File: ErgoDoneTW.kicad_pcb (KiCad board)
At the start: 2 copper layers, 182.8 x 158.9 mm, 71 parts, among them J1 3.5mm, J2 USB_C, P1 hole_r1.75, P2 hole_r1.75, P3 hole_r1.75, P4 hole_r1.75, P5 hole_r1.75, P6 hole_r1.75, P7 hole_r1.75, P8 hole_r1.75, SW0:10 SW0:3, SW0:11 SW0:2, SW0:12 SW0:1, SW0:7 SW0:6, SW0:8 SW0:5, SW0:9 SW0:4, SW1:10 SW1:3, SW1:11 SW1:2, SW1:12 SW1:1, SW1:13 SW1:0, SW1:9 SW1:4, SW2:10 SW2:3, SW2:11 SW2:2, SW2:12 SW2:1, SW2:13 SW2:0, SW2:7 SW2:6, SW2:8 SW2:5, SW2:9 SW2:4, SW3:10 SW3:3, SW3:11 SW3:2, SW3:12 SW3:1, SW3:13 SW3:0, SW3:8 SW3:5, SW3:9 SW3:4, SW4:10 SW4:3, SW4:11 SW4:2, SW4:12 SW4:1, SW4:13 SW4:0, SW4:7 SW4:6, SW4:8 SW4:5, SW4:9 SW4:4, SW5:10 SW5:3, SW5:11 SW5:2, SW5:12 SW5:1, SW5:13 SW5:0, SW5:7 SW5:6, SW5:8 SW5:5, SW5:9 SW5:4, U2 MCP23018, U4 TEENSY2.0

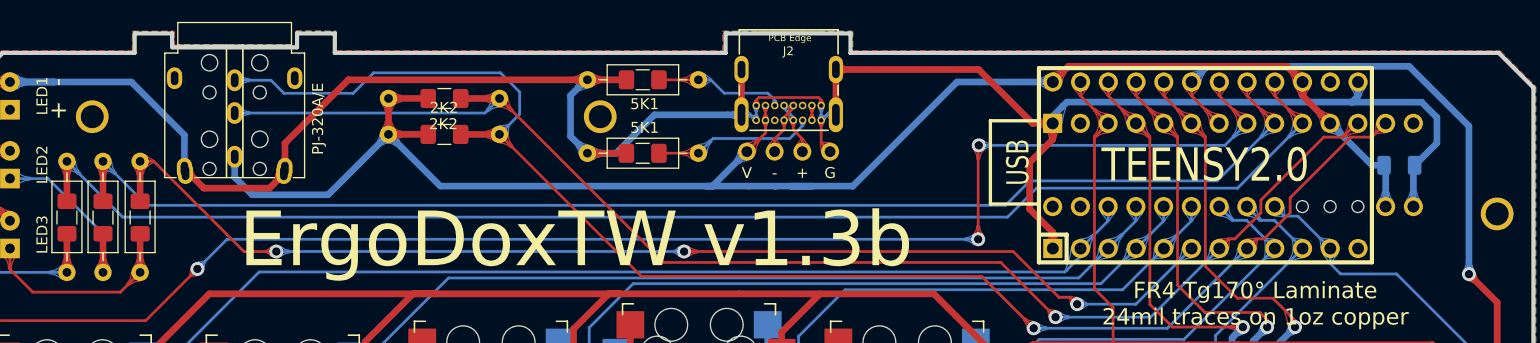
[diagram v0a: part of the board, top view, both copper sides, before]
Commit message: update smd  cap position to avoid conflict with mcp23018
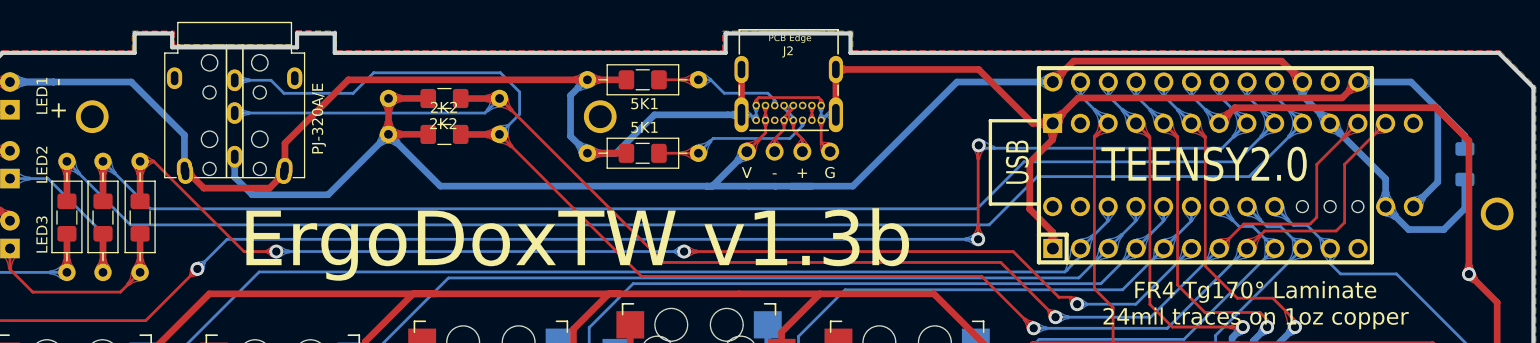
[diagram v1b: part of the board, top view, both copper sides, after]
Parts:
- moved 100nF 6.00 mm to (199.6, 42.5), turned to 90 degrees
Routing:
- net VCC: track 148.6 -> 160.0 mm
- net /ROW1: track 350.7 -> 345.8 mm
- net GND: track 227.6 -> 231.9 mm
- net /SDAM: track 133.3 -> 135.6 mm
- net /SCLM: track 123.6 -> 125.8 mm
- net /LED_A: track 127.2 -> 127.8 mm

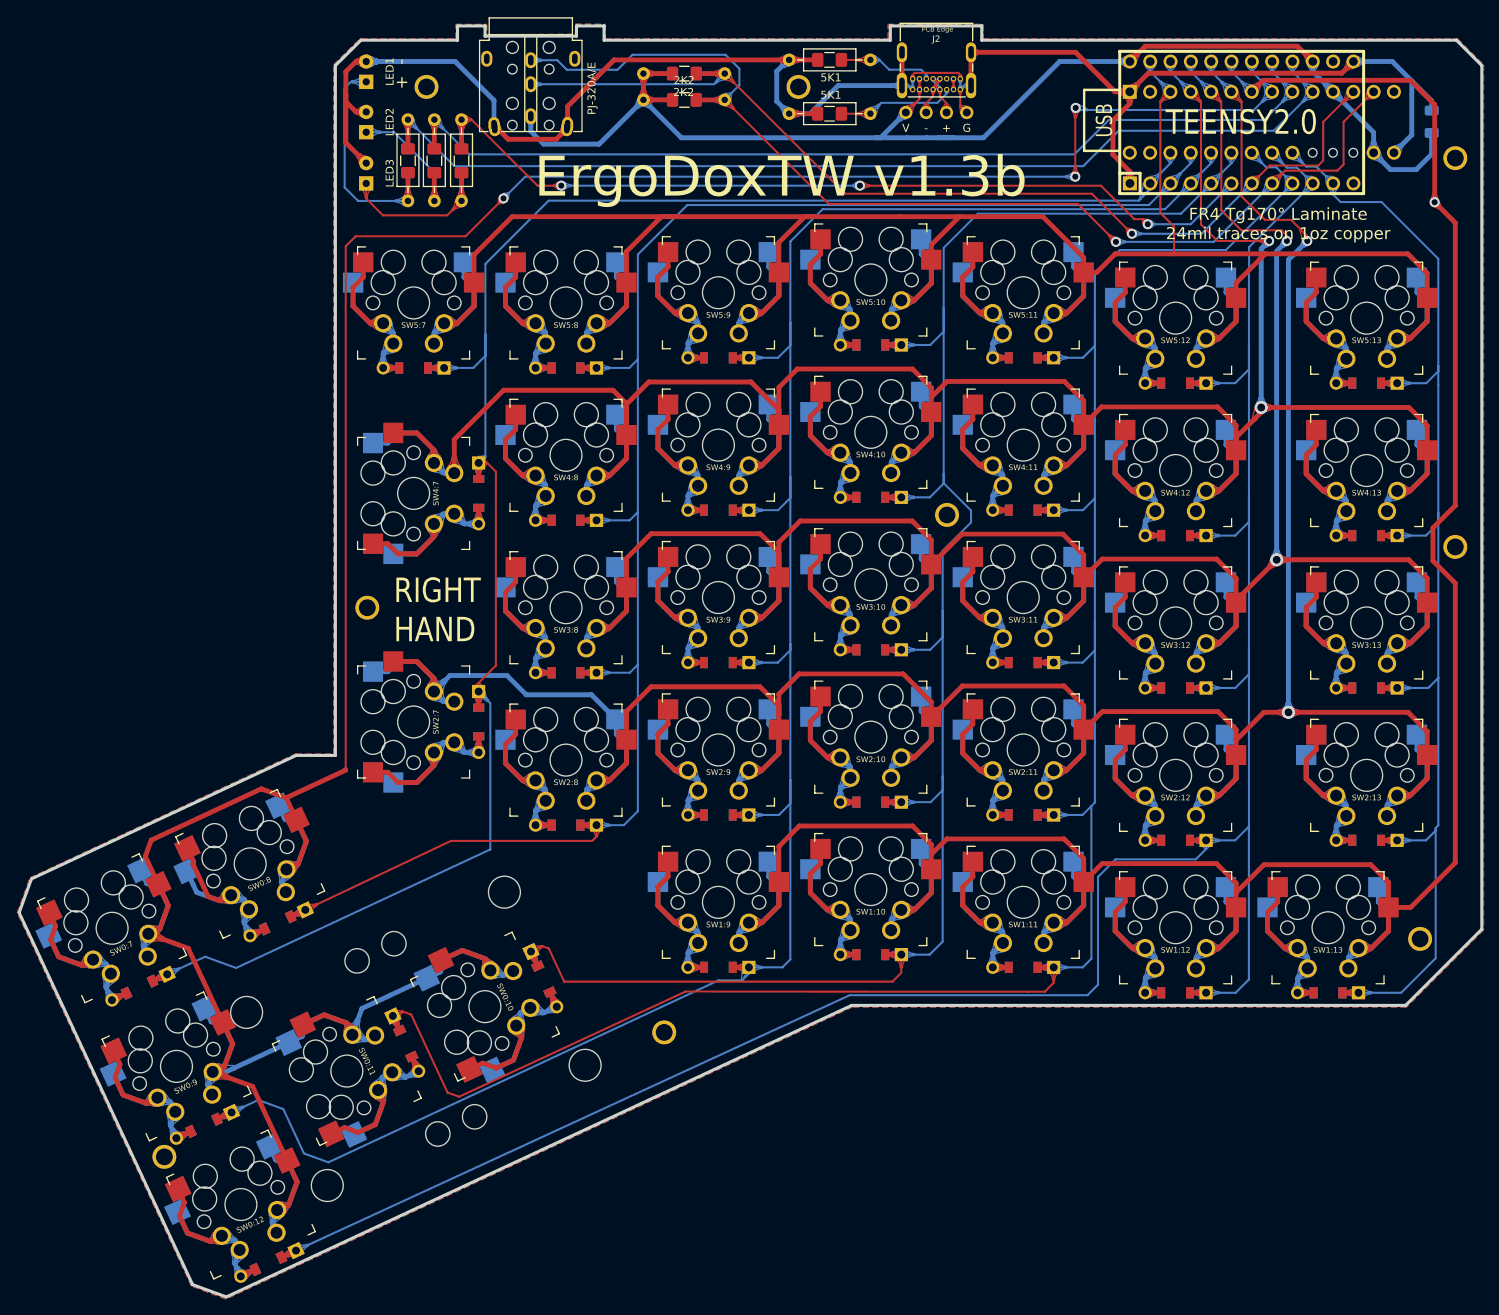
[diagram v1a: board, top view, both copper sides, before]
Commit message: update v1.4
change led / resistor position due to add new drill hole from ErgoDox
for a better support with cases.
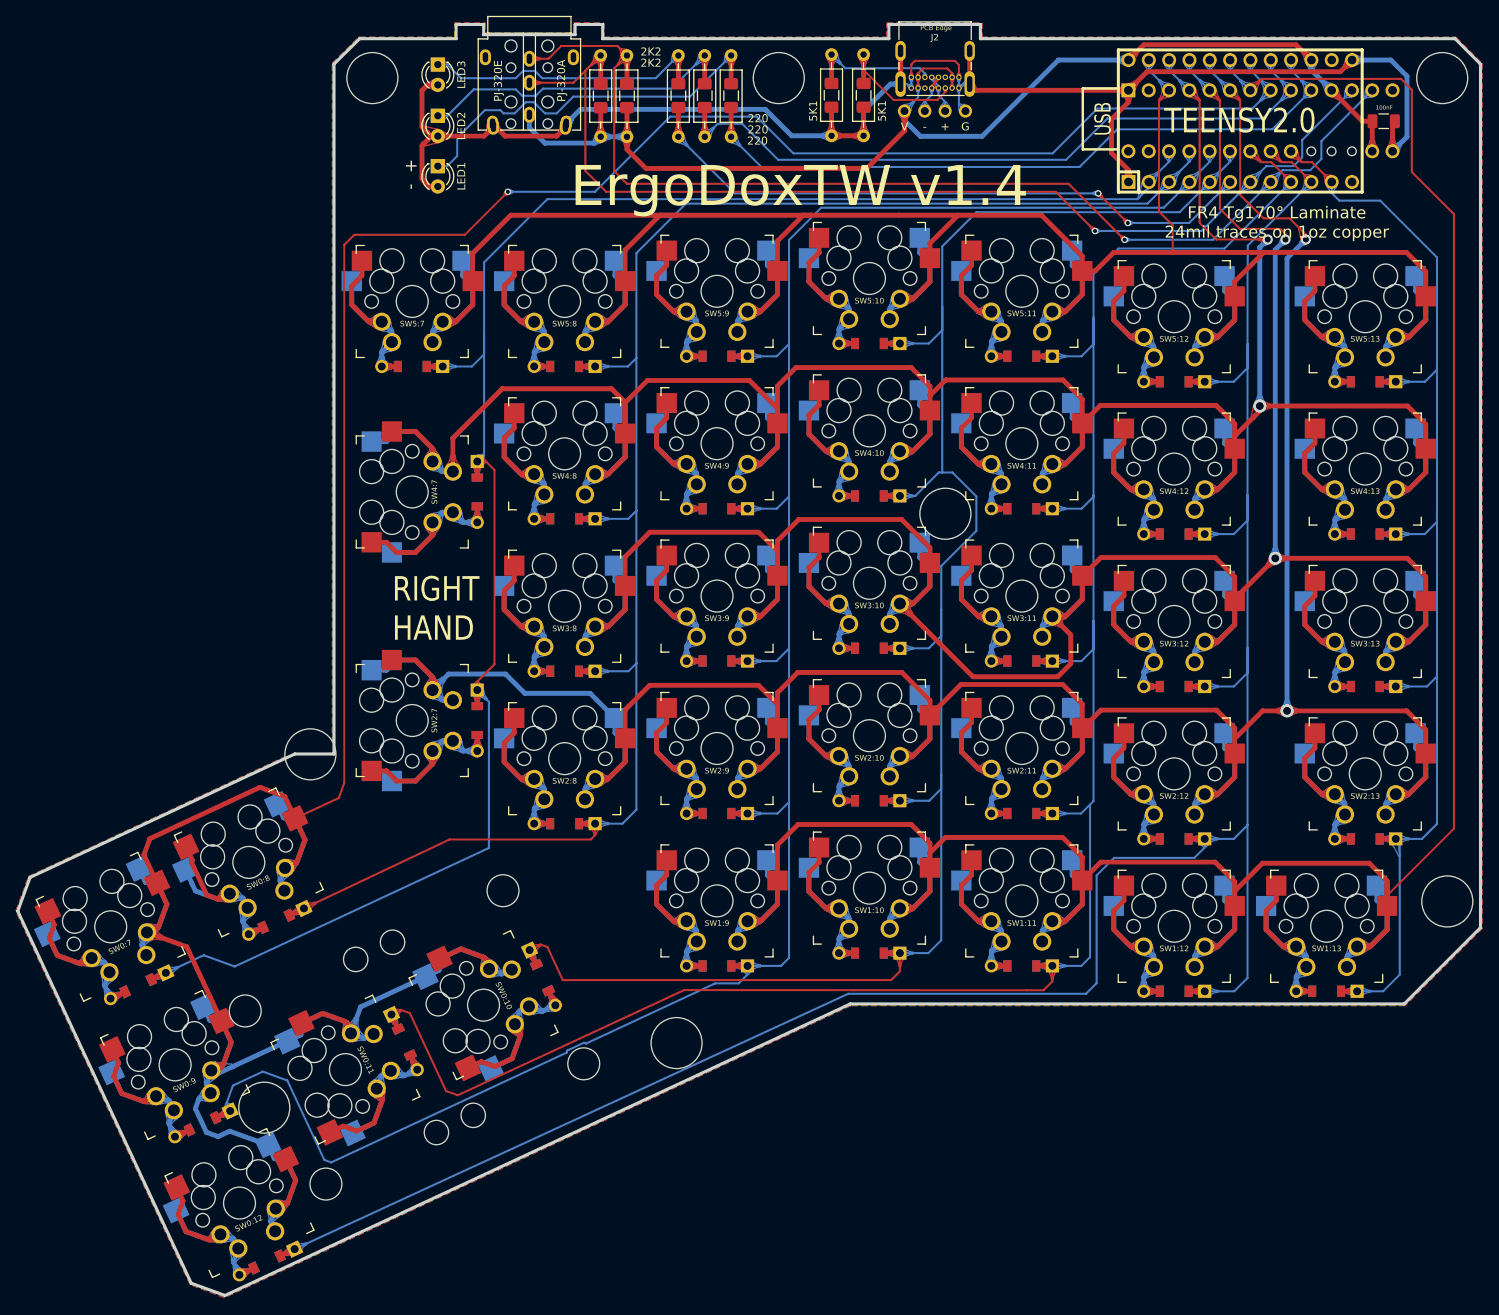
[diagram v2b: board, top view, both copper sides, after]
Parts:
- removed P1, P2, P3, P4, P5, P6, P7, P8, REF**: hole_r1.75, YD_modules:hole_r1.75
- added S3: MEHCINAL, Enhance:ErgoDOXmech, F.Cu at (50.6, 177.7)
- 100nF, LED1, LED2, LED3, R1, R2: moved to F.Cu
- RA2, RB2, RC2: value 2K2 -> 220
- moved RA2 41.2 mm to (112.0, 39.2), turned to 90 degrees
- moved RA1 40.5 mm to (112.0, 44.3), turned to 90 degrees
- moved RB2 34.8 mm to (108.7, 39.2), turned to 90 degrees
- moved RB1 33.9 mm to (108.7, 44.3), turned to 90 degrees
- moved RC2 28.3 mm to (105.4, 39.2), turned to 90 degrees
- moved RC1 27.2 mm to (105.4, 44.3), turned to 90 degrees
- moved LED3 17.3 mm to (75.4, 35.3), turned to 270 degrees
- moved LED1 13.8 mm to (75.4, 48.0), turned to 270 degrees
- moved R6 10.8 mm to (95.7, 39.2), turned to 90 degrees
- moved R2 9.54 mm to (95.7, 44.3), turned to 90 degrees
- moved LED2 9.19 mm to (75.4, 41.7), turned to 270 degrees
- moved R5 7.44 mm to (128.6, 34.1), turned to 270 degrees
- moved R3 7.19 mm to (99.0, 39.2), turned to 90 degrees
- moved 100nF 5.99 mm to (193.6, 42.4), turned to 0 degrees
- moved R1 5.05 mm to (99.0, 44.3), turned to 90 degrees
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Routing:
- net /LED_A: track 127.8 -> 86.5 mm
- net /LED_B: track 120.8 -> 87.9 mm
- net GND: track 231.9 -> 203.7 mm
- net /LED_C: track 107.4 -> 79.2 mm, vias 3 -> 2
- net Net-(LED2-Pad1): track 17.7 -> 40.7 mm
- net Net-(LED1-Pad1): track 27.6 -> 48.7 mm
- net Net-(LED3-Pad1): track 19.0 -> 36.2 mm
- net /SCLM: track 125.8 -> 137.0 mm
- net VCC: track 160.0 -> 149.6 mm
- net /ROW3: track 333.9 -> 341.4 mm
- net /COL4: track 284.8 -> 291.1 mm
- net Net-(J2-PadB5): track 11.9 -> 16.8 mm
- net /COL0: track 168.5 -> 163.9 mm
- net /SDAM: track 135.6 -> 139.4 mm
- net Net-(J2-PadA5): track 14.7 -> 18.2 mm
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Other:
- rule via_min_size: 0.4064 -> 0.508
- board text added: "ErgoDoxTW v1.4"
- board text removed: "ErgoDoxTW v1.3b"
